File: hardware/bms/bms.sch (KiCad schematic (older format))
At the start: 1 part

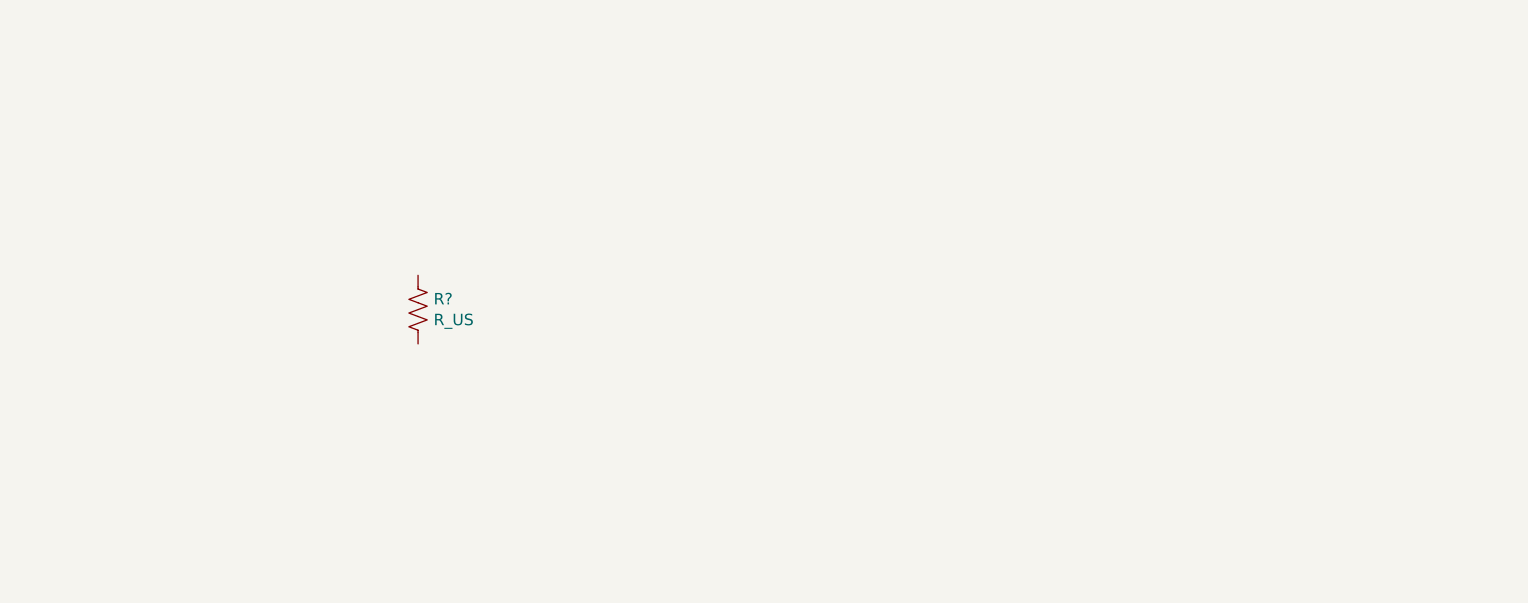
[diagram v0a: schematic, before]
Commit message: added template sch pages
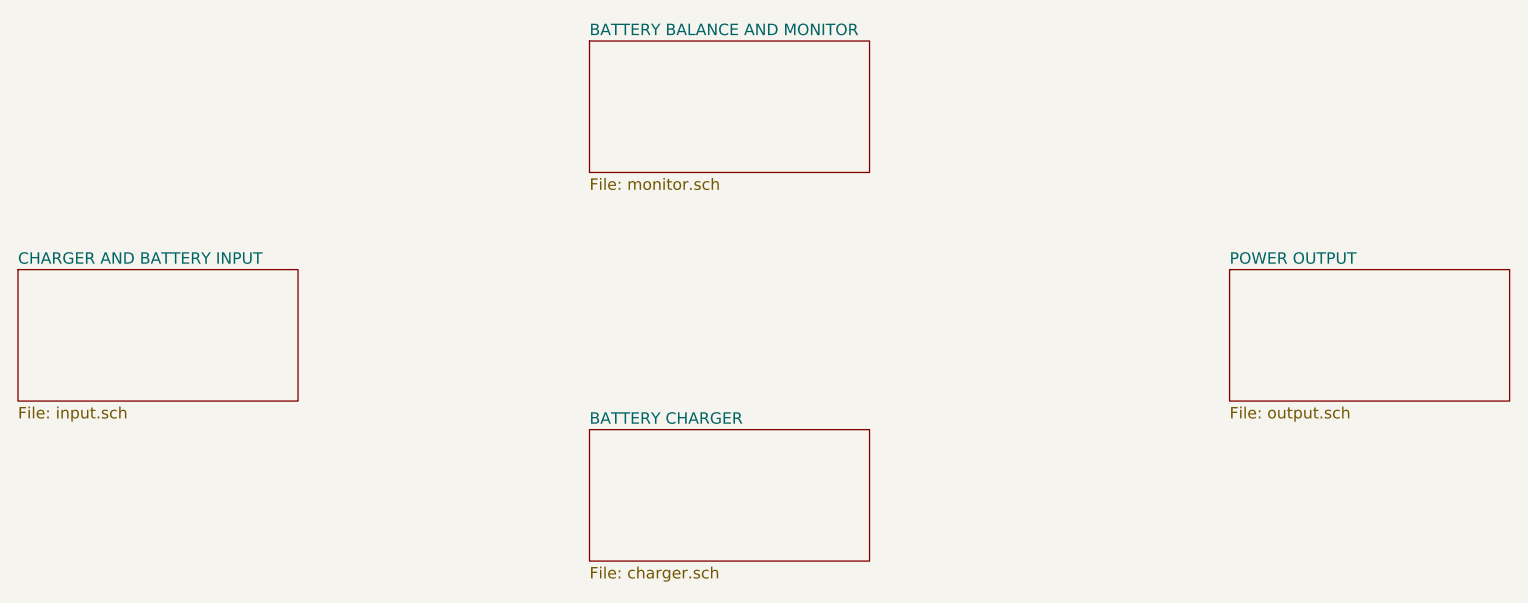
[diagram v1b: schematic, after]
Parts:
- removed R?: R_US, symbol Device:R_US
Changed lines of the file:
@@
 $Descr A4 11693 8268
 encoding utf-8
-Sheet 1 1
+Sheet 1 3
 Title ""
 Date ""
@@
 Comment4 ""
 $EndDescr
-$Comp
-L Device:R_US R?
-U 1 1 65238C65
-P 4450 2775
-F 0 "R?" H 4518 2821 50  0000 L CNN
-F 1 "R_US" H 4518 2730 50  0000 L CNN
-F 2 "" V 4490 2765 50  0001 C CNN
-F 3 "~" H 4450 2775 50  0001 C CNN
-	1    4450 2775
-	1    0    0    -1
-$EndComp
+$Sheet
+S 2700 2600 1225 575
+U 6523946B
+F0 "CHARGER AND BATTERY INPUT" 50
+F1 "input.sch" 50
+$EndSheet
+$Sheet
+S 8000 2600 1225 575
+U 65239C4F
+F0 "POWER OUTPUT" 50
+F1 "output.sch" 50
+$EndSheet
+$Sheet
+S 5200 1600 1225 575
+U 6523A805
+F0 "BATTERY BALANCE AND MONITOR" 50
+F1 "monitor.sch" 50
+$EndSheet
+$Sheet
+S 5200 3300 1225 575
+U 6523AB32
+F0 "BATTERY CHARGER" 50
+F1 "charger.sch" 50
+$EndSheet
 $EndSCHEMATC

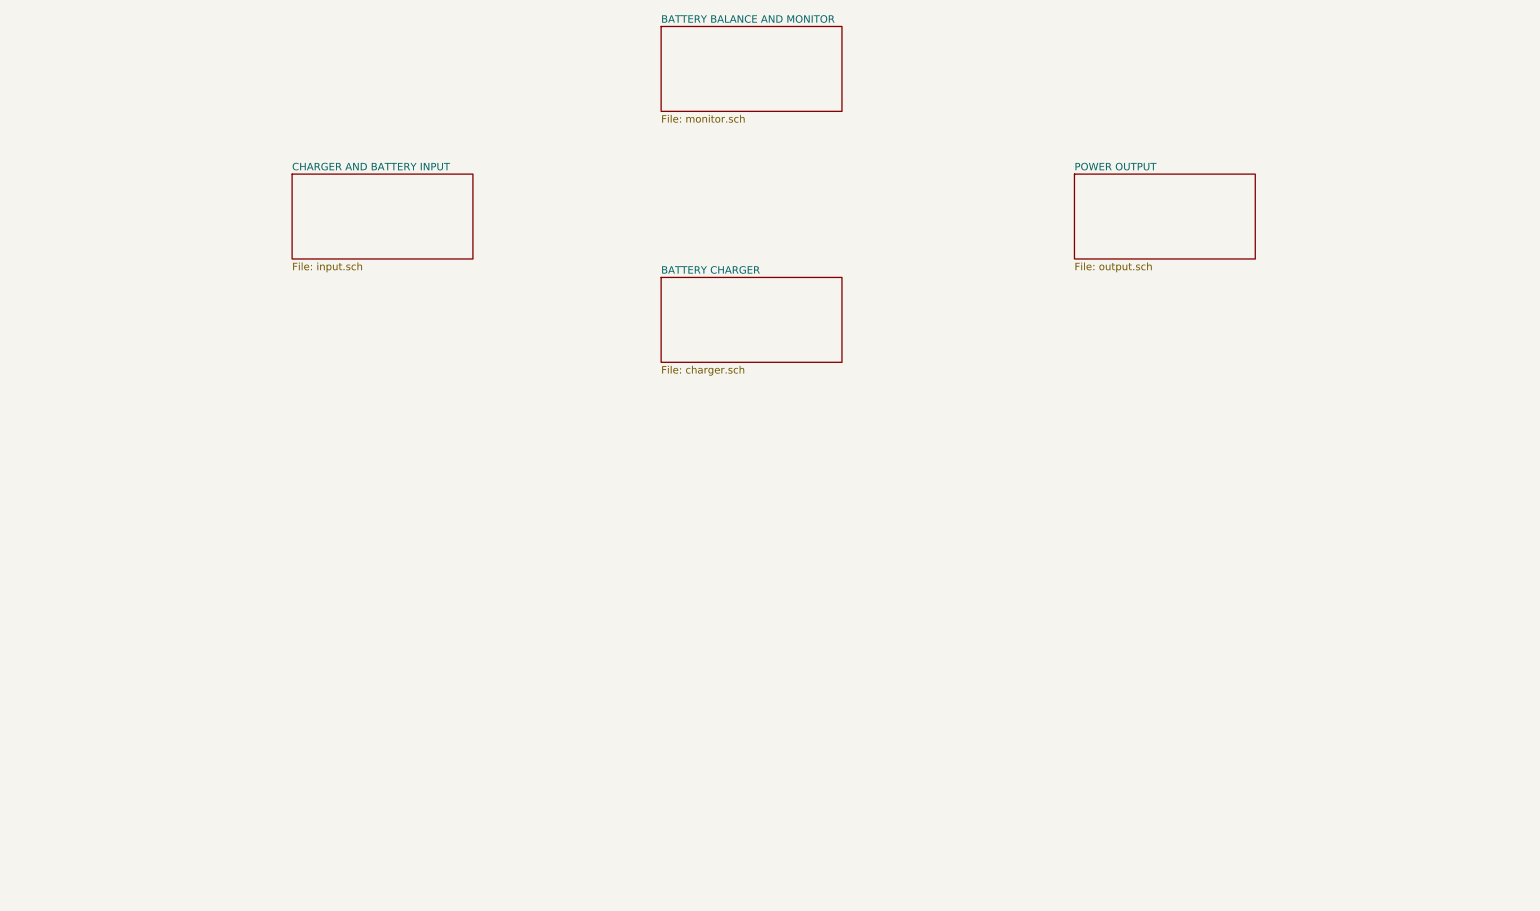
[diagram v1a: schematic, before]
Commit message: Created battery manager and charger IC symbols.
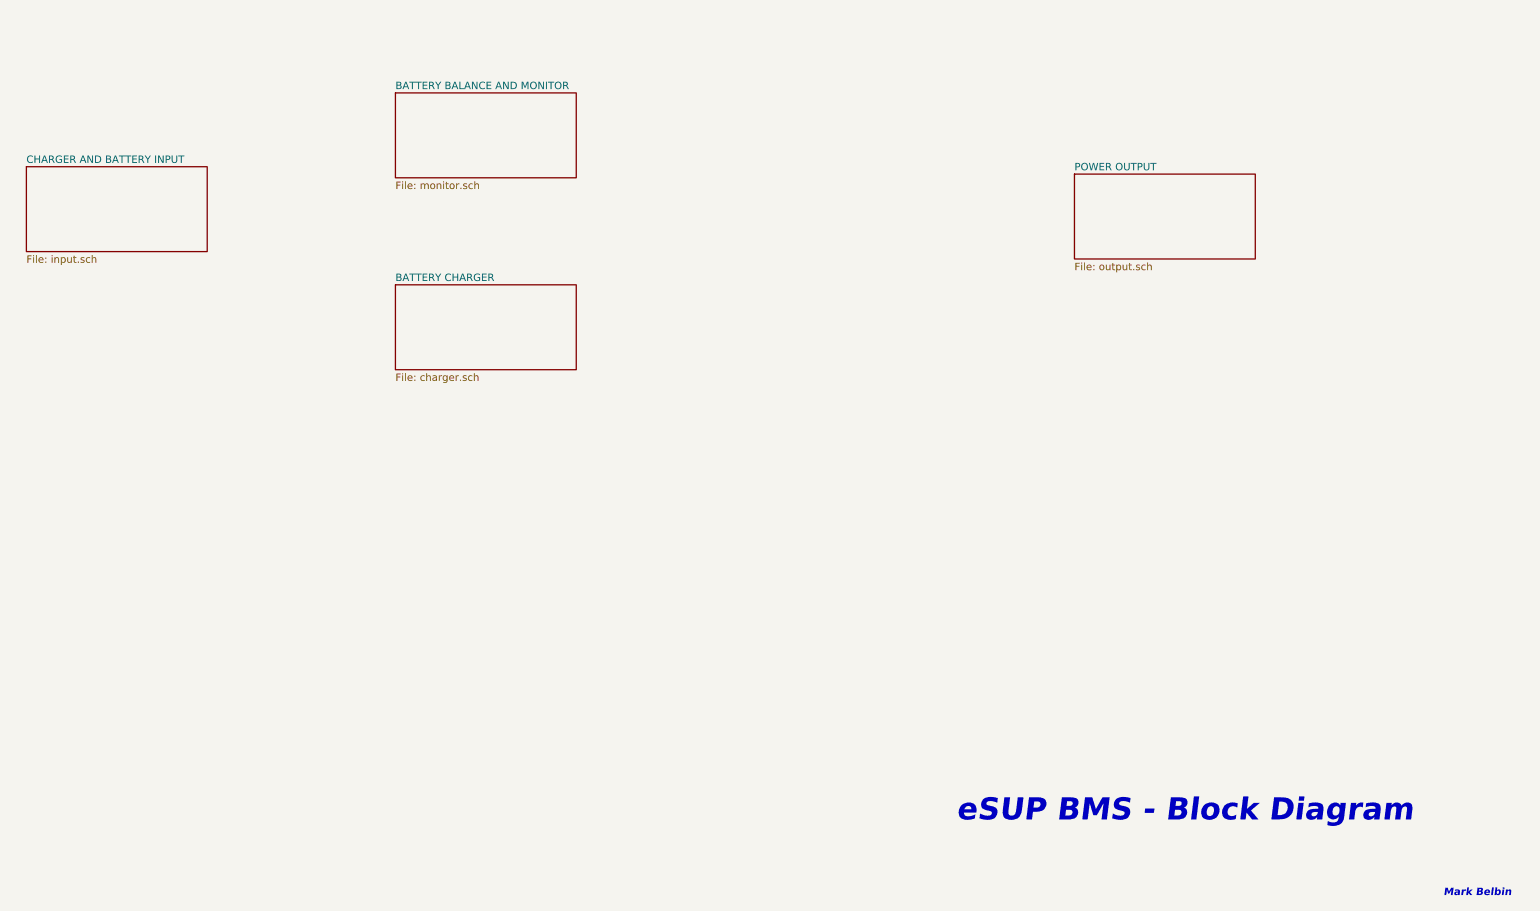
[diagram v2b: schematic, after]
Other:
- note added: "Mark Belbin"
- note added: "eSUP BMS - Block Diagram"
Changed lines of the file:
@@
 $Descr A4 11693 8268
 encoding utf-8
-Sheet 1 3
-Title ""
-Date ""
-Rev ""
+Sheet 1 5
+Title "eSUP - BMS + Charger Board"
+Date "2023-10-09"
+Rev "V1"
 Comp ""
 Comment1 ""
@@
 $EndDescr
 $Sheet
-S 2700 2600 1225 575
-U 6523946B
-F0 "CHARGER AND BATTERY INPUT" 50
-F1 "input.sch" 50
-$EndSheet
-$Sheet
 S 8000 2600 1225 575
 U 65239C4F
@@
 $EndSheet
 $Sheet
-S 5200 1600 1225 575
+S 3400 2050 1225 575
 U 6523A805
 F0 "BATTERY BALANCE AND MONITOR" 50
@@
 $EndSheet
 $Sheet
-S 5200 3300 1225 575
+S 3400 3350 1225 575
 U 6523AB32
 F0 "BATTERY CHARGER" 50
 F1 "charger.sch" 50
 $EndSheet
+$Sheet
+S 900  2550 1225 575
+U 6523946B
+F0 "CHARGER AND BATTERY INPUT" 50
+F1 "input.sch" 50
+$EndSheet
+Text Notes 7200 7000 0    150  Italic 30
+eSUP BMS - Block Diagram
+Text Notes 10500 7500 0    50   Italic 10
+Mark Belbin
 $EndSCHEMATC

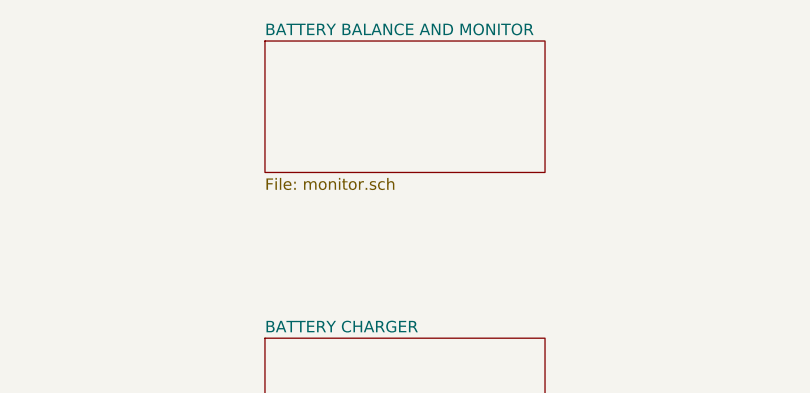
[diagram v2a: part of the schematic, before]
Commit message: More progress on battery management circuit
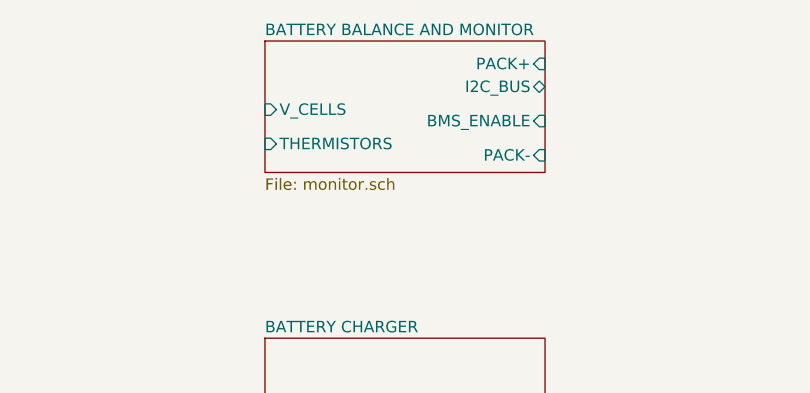
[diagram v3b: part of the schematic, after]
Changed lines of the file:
@@
 F0 "BATTERY BALANCE AND MONITOR" 50
 F1 "monitor.sch" 50
+F2 "BMS_ENABLE" I R 4625 2400 50
+F3 "I2C_BUS" B R 4625 2250 50
+F4 "THERMISTORS" I L 3400 2500 50
+F5 "V_CELLS" I L 3400 2350 50
+F6 "PACK+" I R 4625 2150 50
+F7 "PACK-" I R 4625 2550 50
 $EndSheet
 $Sheet

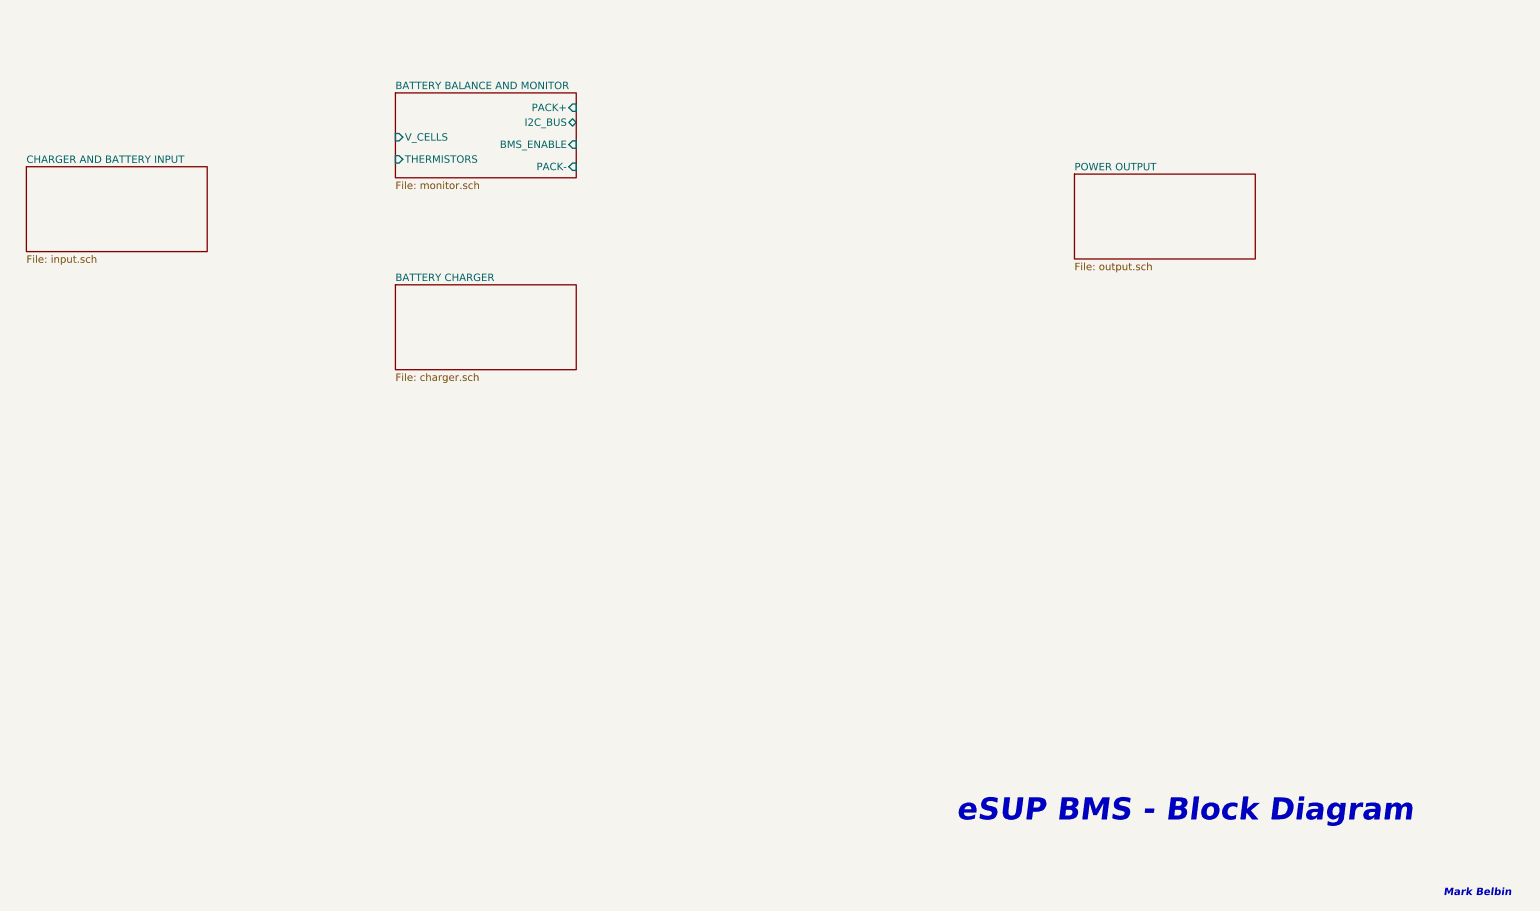
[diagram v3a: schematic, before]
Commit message: Battery monitor / balancer schematic complete. Charger is next. Thinking of adding MCU directly to this board if layout space allows, probably doesn't deserve its own board (or just deserves a dev board)
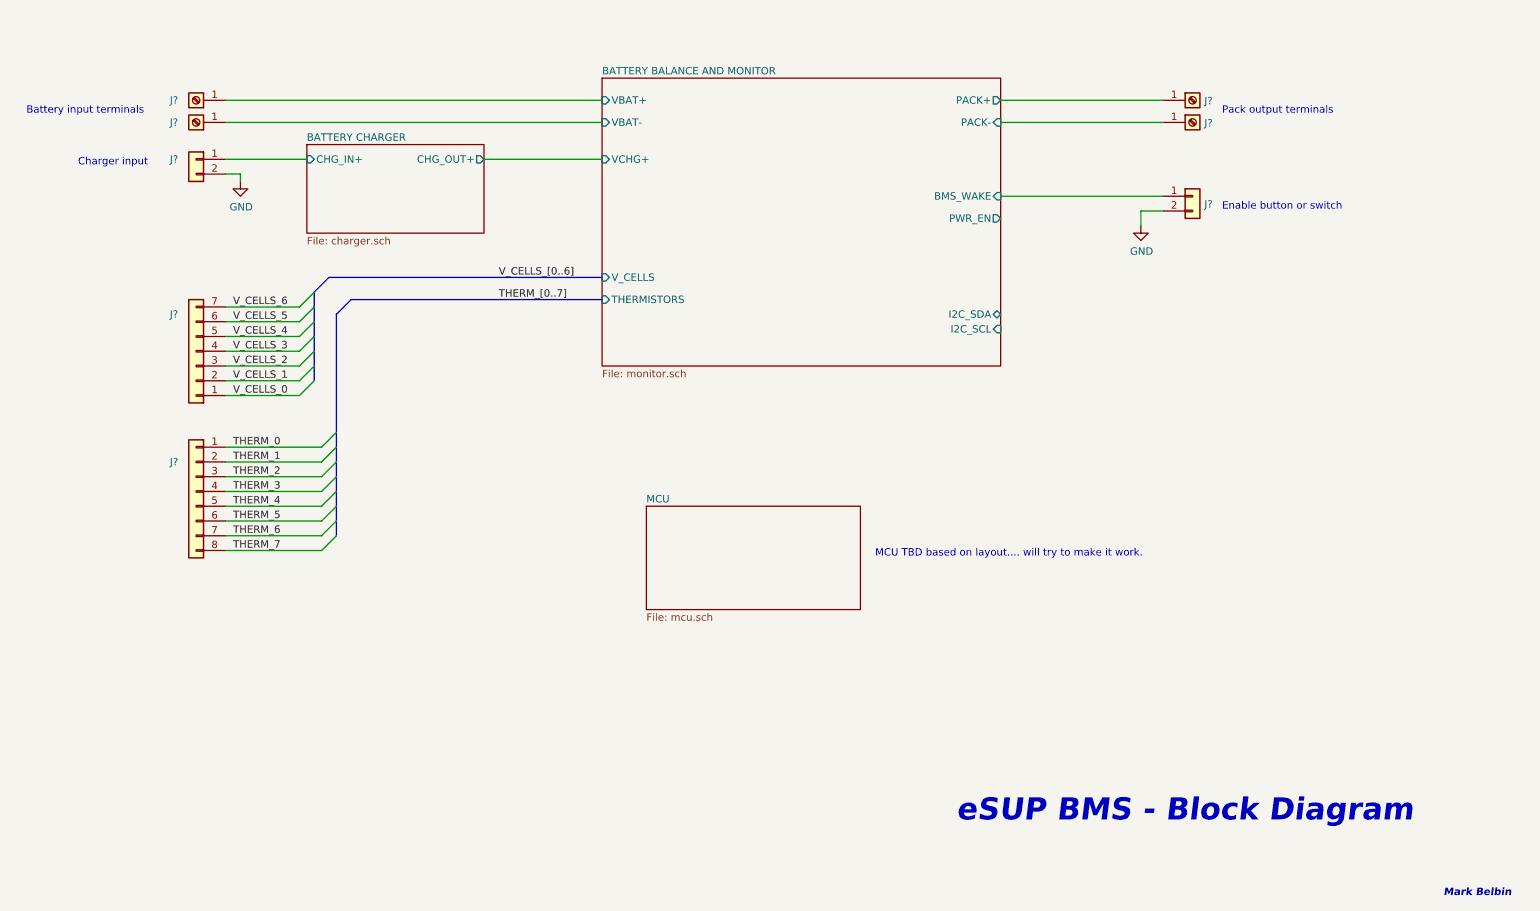
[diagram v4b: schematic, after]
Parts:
- added J? (x4): Screw_Terminal_01x01, symbol Connector:Screw_Terminal_01x01
- added J? (x2): Conn_01x02, symbol Connector_Generic:Conn_01x02
- added J?: Conn_01x08, symbol Connector_Generic:Conn_01x08
- added J?: Conn_01x07, symbol Connector_Generic:Conn_01x07
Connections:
- net BATTERY BALANCE AND MONITOR/PACK+: now also J?.1 (Pin_1)
- net BATTERY BALANCE AND MONITOR/PACK-: now also J?.1 (Pin_1)
- new net BATTERY BALANCE AND MONITOR/BMS_WAKE: J?.1 (Pin_1)
- new net BATTERY BALANCE AND MONITOR/VBAT+: J?.1 (Pin_1)
- new net BATTERY BALANCE AND MONITOR/VBAT-: J?.1 (Pin_1)
- new net BATTERY CHARGER/CHG_IN+: J?.1 (Pin_1)
- new net GND: J?.2 (Pin_2), J?.2 (Pin_2)
- new net THERM_0: J?.1 (Pin_1)
- new net THERM_1: J?.2 (Pin_2)
- new net THERM_2: J?.3 (Pin_3)
- new net THERM_3: J?.4 (Pin_4)
- new net THERM_4: J?.5 (Pin_5)
- new net THERM_5: J?.6 (Pin_6)
- new net THERM_6: J?.7 (Pin_7)
- new net THERM_7: J?.8 (Pin_8)
- new net V_CELLS_0: J?.1 (Pin_1)
- new net V_CELLS_1: J?.2 (Pin_2)
- new net V_CELLS_2: J?.3 (Pin_3)
- new net V_CELLS_3: J?.4 (Pin_4)
- new net V_CELLS_4: J?.5 (Pin_5)
- new net V_CELLS_5: J?.6 (Pin_6)
- new net V_CELLS_6: J?.7 (Pin_7)
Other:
- note added: "Battery input terminals"
- note added: "Charger input"
- note added: "Enable button or switch"
- note added: "MCU TBD based on layout.... will try to make it work."
- note added: "Pack output terminals"
